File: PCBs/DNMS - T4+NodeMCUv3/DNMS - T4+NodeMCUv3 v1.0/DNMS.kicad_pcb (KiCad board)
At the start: 2 copper layers, 61 x 32.5 mm, 23 parts, among them J1 Conn_01x06, J2 Conn_01x02, J3 Conn_01x04, J4 Conn_01x05, J5 Conn_01x06, J6 Conn_01x05, U2 NodeMCU V3, U3 Teensy4.0

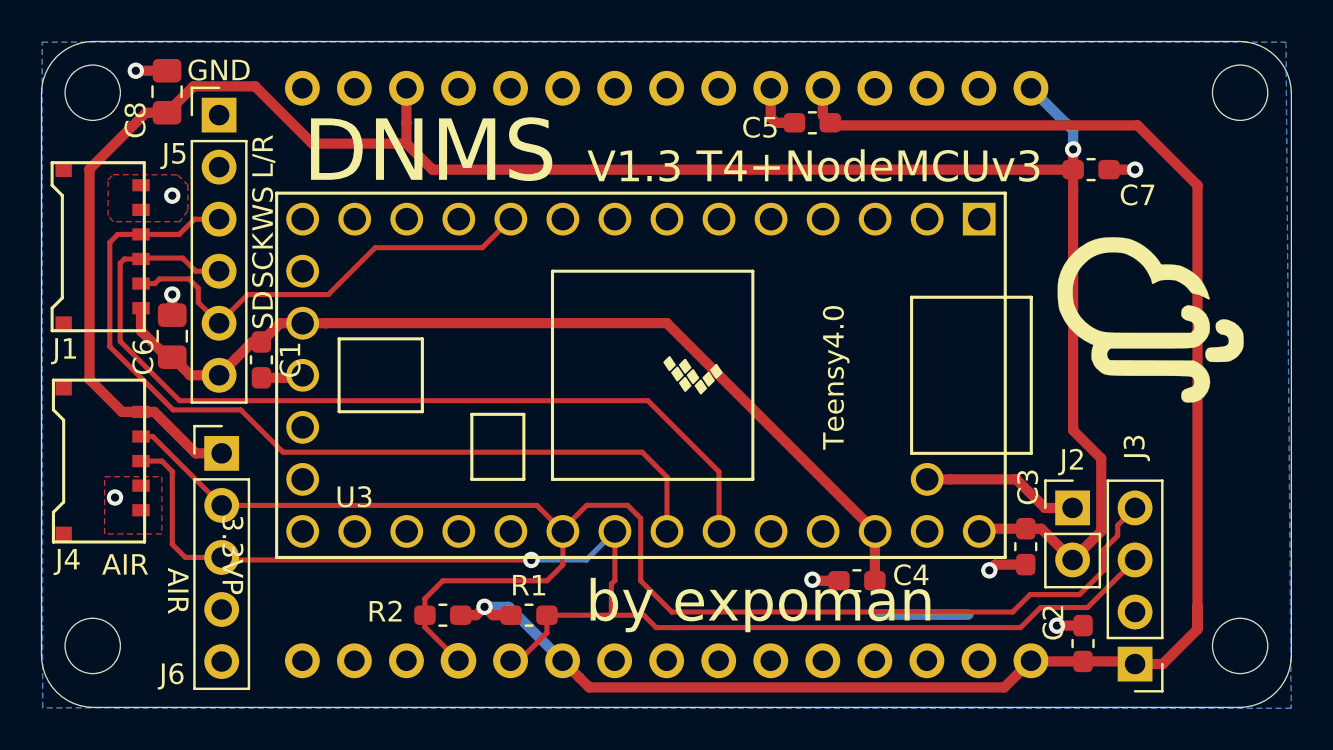
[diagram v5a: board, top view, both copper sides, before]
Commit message: move mounting holes
increase diameter of holes to 3.2mm
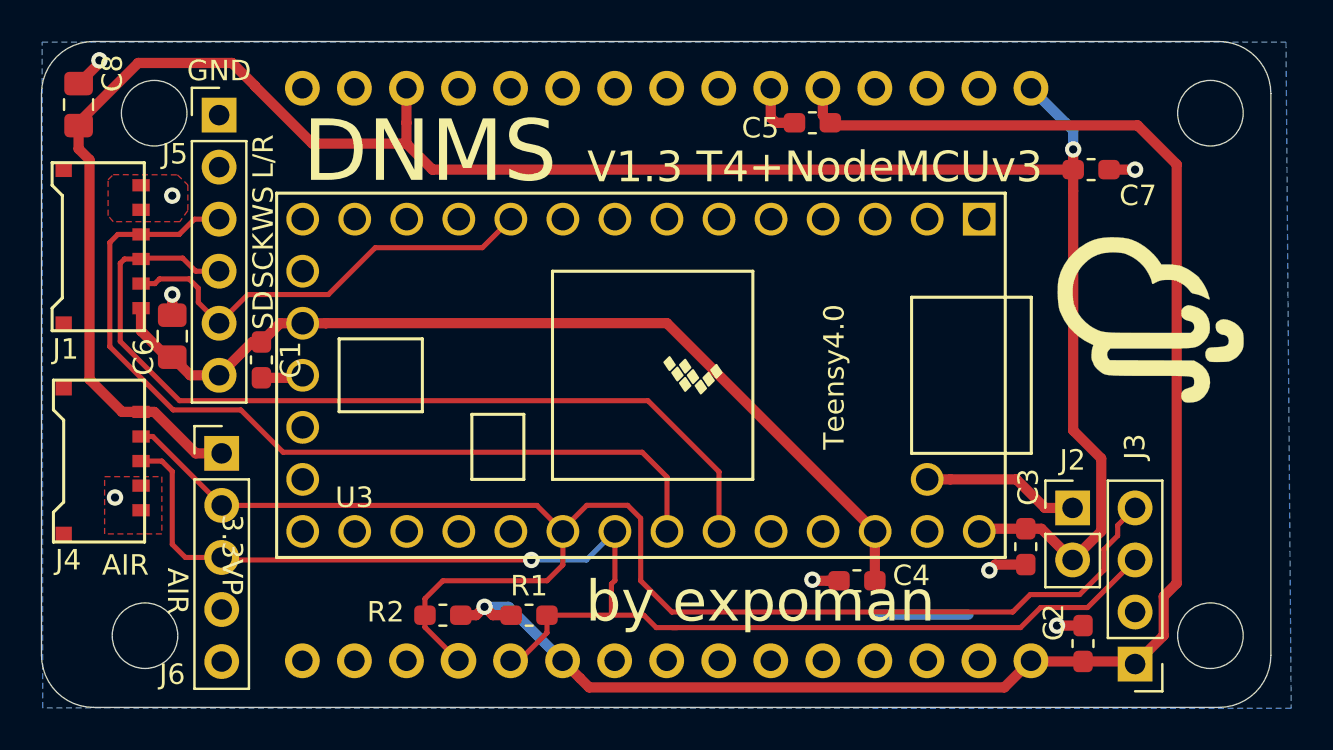
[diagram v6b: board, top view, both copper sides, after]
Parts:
- removed the REF1 at (124.0, 60.0)
- removed the REF1 at (68.0, 60.0)
- added REF1: MountingHole_2.7mm_M2.5, MountingHole:MountingHole_2.7mm_M2.5, F.Cu at (122.5, 61.0)
- added REF1: MountingHole_2.7mm_M2.5, MountingHole:MountingHole_2.7mm_M2.5, F.Cu at (71.0, 60.0)
- moved C8 4.36 mm to (67.3, 60.6)
- moved REF1 0.84 mm to (67.9, 86.2)
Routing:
- net +5V: track 102.6 -> 105.6 mm
- net +3V3: track 84.7 -> 82.0 mm
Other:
- board size 61 x 32.5 mm -> 60 x 32.5 mm
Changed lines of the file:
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@@
     (thickness 1.6)
     (drawings 19)
-    (tracks 194)
+    (tracks 198)
     (zones 0)
     (modules 23)
@@
     (mod_text_size 1 1)
     (mod_text_width 0.15)
-    (pad_size 0.6 0.85)
-    (pad_drill 0)
+    (pad_size 3.2 3.2)
+    (pad_drill 3.2)
     (pad_to_mask_clearance 0.051)
     (solder_mask_min_width 0.25)
@@
   )
   (module Capacitor_SMD:C_0805_2012Metric_Pad1.15x1.40mm_HandSolder (layer F.Cu)
-    (at 71.628 59.953 90)
+    (at 67.31 60.579 90)
     (descr "Capacitor SMD 0805 (2012 Metric), square (rectangular) end terminal, IPC_7351 nominal with elongated pad for handsoldering. (Body size source: https://docs.google.com/spreadsheets/d/1BsfQQcO9C6DZCsRaXUlFlo91Tg2WpOkGARC1WS5S8t0/edit?usp=sharing), generated with kicad-footprint-generator")
     (tags "capacitor handsolder")
     (attr smd)
-    (fp_text reference C8 (at -1.388 -1.524 90) (layer F.SilkS)
+    (fp_text reference C8 (at 1.524 1.651 90) (layer F.SilkS)
       (effects (font (size 1 1) (thickness 0.15)))
     )
@@
   )
   (module MountingHole:MountingHole_2.7mm_M2.5 (layer F.Cu)
-    (at 124 60)
+    (at 122.55 61)
     (descr "Mounting Hole 2.7mm, no annular, M2.5")
     (tags "mounting hole 2.7mm no annular m2.5")
@@
     (fp_circle (center 0 0) (end 2.7 0) (layer Cmts.User) (width 0.15))
     (fp_circle (center 0 0) (end 2.95 0) (layer F.CrtYd) (width 0.05))
-    (pad 1 np_thru_hole circle (at 0 0) (size 2.7 2.7) (drill 2.7) (layers *.Cu *.Mask))
+    (pad "" np_thru_hole circle (at 0 0) (size 3.2 3.2) (drill 3.2) (layers *.Cu *.Mask))
   )
   (module MountingHole:MountingHole_2.7mm_M2.5 (layer F.Cu)
@@
     (fp_circle (center 0 0) (end 2.7 0) (layer Cmts.User) (width 0.15))
     (fp_circle (center 0 0) (end 2.95 0) (layer F.CrtYd) (width 0.05))
-    (pad 1 np_thru_hole circle (at 0 0) (size 2.7 2.7) (drill 2.7) (layers *.Cu *.Mask))
+    (pad "" np_thru_hole circle (at -1.45 -0.5) (size 3.2 3.2) (drill 3.2) (layers *.Cu *.Mask))
   )
   (module MountingHole:MountingHole_2.7mm_M2.5 (layer F.Cu)
-    (at 68 87)
+    (at 67.875 86.1648)
     (descr "Mounting Hole 2.7mm, no annular, M2.5")
     (tags "mounting hole 2.7mm no annular m2.5")
@@
     (fp_circle (center 0 0) (end 2.7 0) (layer Cmts.User) (width 0.15))
     (fp_circle (center 0 0) (end 2.95 0) (layer F.CrtYd) (width 0.05))
-    (pad 1 np_thru_hole circle (at 0 0) (size 2.7 2.7) (drill 2.7) (layers *.Cu *.Mask))
+    (pad "" np_thru_hole circle (at 2.677 0.3352) (size 3.2 3.2) (drill 3.2) (layers *.Cu *.Mask))
   )
   (module MountingHole:MountingHole_2.7mm_M2.5 (layer F.Cu)
-    (at 68 60)
+    (at 71 60)
     (descr "Mounting Hole 2.7mm, no annular, M2.5")
     (tags "mounting hole 2.7mm no annular m2.5")
@@
     (fp_circle (center 0 0) (end 2.7 0) (layer Cmts.User) (width 0.15))
     (fp_circle (center 0 0) (end 2.95 0) (layer F.CrtYd) (width 0.05))
-    (pad 1 np_thru_hole circle (at 0 0) (size 2.7 2.7) (drill 2.7) (layers *.Cu *.Mask))
+    (pad "" np_thru_hole circle (at 0 1) (size 3.2 3.2) (drill 3.2) (layers *.Cu *.Mask))
   )
   (module "logos eigene:logo luftdaten.info" (layer F.Cu)
@@
   )
   (gr_line (start 65.5 60.04) (end 65.5 87.46) (layer Edge.Cuts) (width 0.05))
-  (gr_line (start 126.5 60.04) (end 126.5 87.46) (layer Edge.Cuts) (width 0.05))
-  (gr_line (start 123.96 90) (end 68.04 90) (layer Edge.Cuts) (width 0.05))
-  (gr_line (start 68.04 57.5) (end 123.96 57.5) (layer Edge.Cuts) (width 0.05))
+  (gr_line (start 125.5 60.04) (end 125.5 87.46) (layer Edge.Cuts) (width 0.05))
+  (gr_line (start 122.96 90) (end 68.04 90) (layer Edge.Cuts) (width 0.05))
+  (gr_line (start 68.04 57.5) (end 122.96 57.5) (layer Edge.Cuts) (width 0.05))
   (gr_arc (start 68.04 60.04) (end 68.04 57.5) (angle -90) (layer Edge.Cuts) (width 0.05))
   (gr_arc (start 68.04 87.46) (end 65.5 87.46) (angle -90) (layer Edge.Cuts) (width 0.05))
-  (gr_arc (start 123.96 87.46) (end 123.96 90) (angle -90) (layer Edge.Cuts) (width 0.05))
-  (gr_arc (start 123.96 60.04) (end 126.5 60.04) (angle -90) (layer Edge.Cuts) (width 0.05))
+  (gr_arc (start 122.96 87.46) (end 122.96 90) (angle -90) (layer Edge.Cuts) (width 0.05))
+  (gr_arc (start 122.96 60.04) (end 125.5 60.04) (angle -90) (layer Edge.Cuts) (width 0.05))
   (gr_text "V1.3 T4+NodeMCUv3" (at 103.251 63.627) (layer F.SilkS)
     (effects (font (size 1.5 1.5) (thickness 0.3)))
@@
   (segment (start 78.12474 73.914) (end 78.24724 73.7915) (width 0.5) (layer F.Cu) (net 1))
   (segment (start 76.234 73.914) (end 78.12474 73.914) (width 0.5) (layer F.Cu) (net 1))
-  (via (at 70.104 58.928) (size 0.8) (drill 0.4) (layers F.Cu B.Cu) (net 1))
-  (segment (start 71.628 58.928) (end 70.104 58.928) (width 0.5) (layer F.Cu) (net 1))
   (segment (start 101.092 61.214) (end 101.092 59.78398) (width 0.5) (layer F.Cu) (net 1))
   (segment (start 102.249 61.468) (end 101.346 61.468) (width 0.5) (layer F.Cu) (net 1))
@@
   (segment (start 117.602 63.754) (end 118.872 63.754) (width 0.5) (layer F.Cu) (net 1))
   (via (at 118.872 63.754) (size 0.8) (drill 0.4) (layers F.Cu B.Cu) (net 1))
+  (via (at 68.326 58.42) (size 0.8) (drill 0.4) (layers F.Cu B.Cu) (net 1))
+  (segment (start 68.326 58.547) (end 68.326 58.42) (width 0.5) (layer F.Cu) (net 1))
+  (segment (start 67.31 59.554) (end 67.319 59.554) (width 0.5) (layer F.Cu) (net 1))
+  (segment (start 67.319 59.554) (end 68.326 58.547) (width 0.5) (layer F.Cu) (net 1))
   (segment (start 85.852 85.584) (end 85.965 85.471) (width 0.25) (layer F.Cu) (net 2))
   (segment (start 88.392 85.499) (end 88.42 85.471) (width 0.25) (layer F.Cu) (net 2))
@@
   (segment (start 116.332 87.757) (end 118.745 87.757) (width 0.5) (layer F.Cu) (net 2))
   (segment (start 119.0244 87.7316) (end 118.872 87.884) (width 0.5) (layer F.Cu) (net 2))
-  (segment (start 121.92 86.186) (end 121.92 85.09) (width 0.5) (layer F.Cu) (net 2))
-  (segment (start 120.222 87.884) (end 121.92 86.186) (width 0.5) (layer F.Cu) (net 2))
-  (segment (start 118.872 87.884) (end 120.222 87.884) (width 0.5) (layer F.Cu) (net 2))
-  (segment (start 121.92 86.106) (end 121.92 85.09) (width 0.5) (layer F.Cu) (net 2))
   (segment (start 104.113939 61.468) (end 103.999 61.468) (width 0.5) (layer F.Cu) (net 2))
+  (segment (start 104.240939 61.595) (end 104.113939 61.468) (width 0.5) (layer F.Cu) (net 2))
   (segment (start 118.999 61.595) (end 104.240939 61.595) (width 0.5) (layer F.Cu) (net 2))
-  (segment (start 121.92 85.09) (end 121.92 64.516) (width 0.5) (layer F.Cu) (net 2))
-  (segment (start 104.240939 61.595) (end 104.113939 61.468) (width 0.5) (layer F.Cu) (net 2))
-  (segment (start 121.92 64.516) (end 118.999 61.595) (width 0.5) (layer F.Cu) (net 2))
+  (segment (start 120.269 86.487) (end 120.269 84.582) (width 0.5) (layer F.Cu) (net 2))
+  (segment (start 118.872 87.884) (end 120.269 86.487) (width 0.5) (layer F.Cu) (net 2))
+  (segment (start 120.269 84.582) (end 120.904 83.947) (width 0.5) (layer F.Cu) (net 2))
+  (segment (start 120.904 83.947) (end 120.904 63.5) (width 0.5) (layer F.Cu) (net 2))
+  (segment (start 120.904 63.5) (end 118.999 61.595) (width 0.5) (layer F.Cu) (net 2))
   (segment (start 83.312 59.78398) (end 83.312 61.468) (width 0.5) (layer F.Cu) (net 3))
   (segment (start 83.312 61.468) (end 83.312 62.484) (width 0.5) (layer F.Cu) (net 3))
   (segment (start 111.252 81.42674) (end 111.26724 81.4115) (width 0.5) (layer F.Cu) (net 3))
   (segment (start 115.824 82.804) (end 114.3 81.28) (width 0.5) (layer F.Cu) (net 3))
-  (segment (start 78.722751 62.484) (end 83.312 62.484) (width 0.5) (layer F.Cu) (net 3))
-  (segment (start 75.928751 59.69) (end 78.722751 62.484) (width 0.5) (layer F.Cu) (net 3))
-  (segment (start 71.628 60.978) (end 72.916 59.69) (width 0.5) (layer F.Cu) (net 3))
-  (segment (start 72.916 59.69) (end 75.928751 59.69) (width 0.5) (layer F.Cu) (net 3))
-  (segment (start 67.8434 73.9884) (end 69.433 75.578) (width 0.5) (layer F.Cu) (net 3))
-  (segment (start 69.433 75.578) (end 70.358 75.578) (width 0.5) (layer F.Cu) (net 3))
-  (segment (start 67.8434 63.7286) (end 67.8434 73.9884) (width 0.5) (layer F.Cu) (net 3))
-  (segment (start 71.628 60.978) (end 70.594 60.978) (width 0.5) (layer F.Cu) (net 3))
-  (segment (start 70.594 60.978) (end 67.8434 63.7286) (width 0.5) (layer F.Cu) (net 3))
   (segment (start 73.0295 77.6015) (end 74.295 77.6015) (width 0.5) (layer F.Cu) (net 3))
   (segment (start 70.358 75.578) (end 71.006 75.578) (width 0.5) (layer F.Cu) (net 3))
@@
   (segment (start 115.852 61.84398) (end 115.47602 61.468) (width 0.5) (layer B.Cu) (net 3))
   (segment (start 115.852 62.766) (end 115.852 61.84398) (width 0.5) (layer B.Cu) (net 3))
+  (segment (start 69.433 75.578) (end 70.358 75.578) (width 0.5) (layer F.Cu) (net 3))
+  (segment (start 67.8434 73.9884) (end 69.433 75.578) (width 0.5) (layer F.Cu) (net 3))
+  (segment (start 67.31 61.604) (end 67.31 62.738) (width 0.5) (layer F.Cu) (net 3))
+  (segment (start 67.8434 63.2714) (end 67.8434 73.9884) (width 0.5) (layer F.Cu) (net 3))
+  (segment (start 67.31 62.738) (end 67.8434 63.2714) (width 0.5) (layer F.Cu) (net 3))
+  (segment (start 78.722751 62.484) (end 83.312 62.484) (width 0.5) (layer F.Cu) (net 3))
+  (segment (start 75.928751 59.69) (end 78.722751 62.484) (width 0.5) (layer F.Cu) (net 3))
+  (segment (start 67.31 61.604) (end 67.31 61.456983) (width 0.5) (layer F.Cu) (net 3))
+  (segment (start 67.31 61.456983) (end 70.219983 58.547) (width 0.5) (layer F.Cu) (net 3))
+  (segment (start 70.219983 58.547) (end 74.803 58.547) (width 0.5) (layer F.Cu) (net 3))
+  (segment (start 74.803 58.547) (end 75.928751 59.672751) (width 0.5) (layer F.Cu) (net 3))
+  (segment (start 75.928751 59.672751) (end 75.928751 59.69) (width 0.5) (layer F.Cu) (net 3))
   (segment (start 84.215 86.08698) (end 84.215 85.5) (width 0.25) (layer F.Cu) (net 4))
   (segment (start 85.852 87.72398) (end 84.215 86.08698) (width 0.25) (layer F.Cu) (net 4))

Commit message: change/move text on silkscreen layer
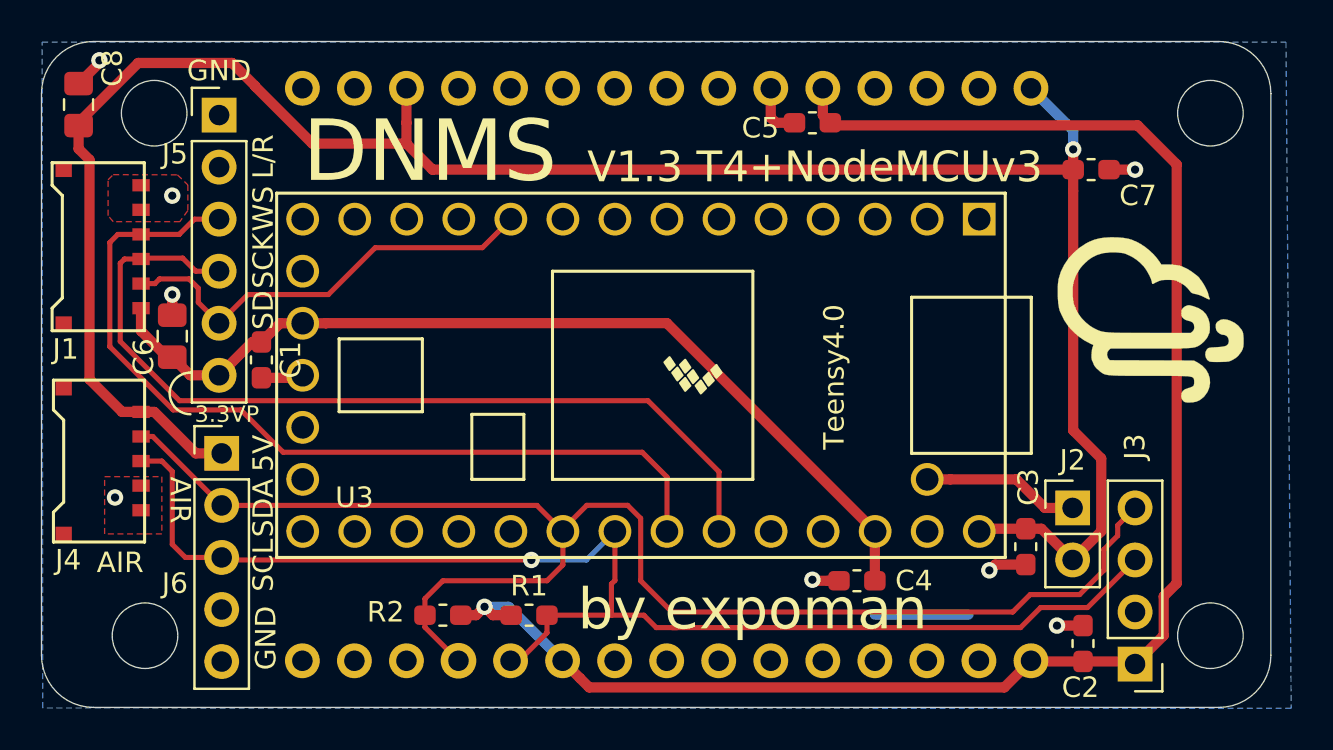
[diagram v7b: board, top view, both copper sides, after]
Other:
- board text added: "5V"
- board text added: "SCL"
- board text added: "SDA"
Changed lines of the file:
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@@
   (general
     (thickness 1.6)
-    (drawings 19)
+    (drawings 24)
     (tracks 198)
     (zones 0)
@@
     (tags "capacitor handsolder")
     (attr smd)
-    (fp_text reference C8 (at 1.524 1.651 90) (layer F.SilkS)
+    (fp_text reference C8 (at 1.778 1.651 90) (layer F.SilkS)
       (effects (font (size 1 1) (thickness 0.15)))
     )
@@
     (descr "Through hole straight pin header, 1x05, 2.54mm pitch, single row")
     (tags "Through hole pin header THT 1x05 2.54mm single row")
-    (fp_text reference J6 (at -2.413 10.7905) (layer F.SilkS)
+    (fp_text reference J6 (at -2.286 6.3455) (layer F.SilkS)
       (effects (font (size 1 1) (thickness 0.15)))
     )
@@
     (tags "capacitor handsolder")
     (attr smd)
-    (fp_text reference C4 (at -2.653 0.254) (layer F.SilkS)
+    (fp_text reference C4 (at -2.78 0) (layer F.SilkS)
       (effects (font (size 1 1) (thickness 0.15)))
     )
@@
     (tags "capacitor handsolder")
     (attr smd)
-    (fp_text reference C2 (at 1.03 -1.43 90) (layer F.SilkS)
+    (fp_text reference C2 (at -2.145 -0.127 180) (layer F.SilkS)
       (effects (font (size 1 1) (thickness 0.15)))
     )
@@
     )
   )
-  (gr_text AIR (at 72.136 84.328 270) (layer F.SilkS)
+  (gr_text GND (at 76.454 86.614 90) (layer F.SilkS)
     (effects (font (size 1 1) (thickness 0.15)))
   )
-  (gr_text AIR (at 69.596 83.058) (layer F.SilkS)
+  (gr_text SCL (at 76.327 83.058 90) (layer F.SilkS)
     (effects (font (size 1 1) (thickness 0.15)))
   )
-  (gr_text "by expoman" (at 100.584 84.836) (layer F.SilkS)
+  (gr_text SDA (at 76.327 80.264 90) (layer F.SilkS)
+    (effects (font (size 1 1) (thickness 0.15)))
+  )
+  (gr_text 5V (at 76.327 77.597 90) (layer F.SilkS)
+    (effects (font (size 1 1) (thickness 0.15)))
+  )
+  (gr_arc (start 72.771 74.676) (end 72.771 73.66) (angle -180) (layer F.SilkS) (width 0.12))
+  (gr_text AIR (at 72.263 79.883 270) (layer F.SilkS)
+    (effects (font (size 1 1) (thickness 0.15)))
+  )
+  (gr_text AIR (at 69.342 82.931) (layer F.SilkS)
+    (effects (font (size 1 1) (thickness 0.15)))
+  )
+  (gr_text "by expoman" (at 100.203 85.217) (layer F.SilkS)
     (effects (font (size 2 2) (thickness 0.3)))
   )
@@
     (effects (font (size 1 1) (thickness 0.15)))
   )
-  (gr_text 3.3VP (at 74.803 82.55 270) (layer F.SilkS)
-    (effects (font (size 1 1) (thickness 0.15)))
+  (gr_text 3.3VP (at 74.549 75.692) (layer F.SilkS)
+    (effects (font (size 0.8 0.8) (thickness 0.15)))
   )
   (gr_text SCK (at 76.327 68.199 90) (layer F.SilkS)
